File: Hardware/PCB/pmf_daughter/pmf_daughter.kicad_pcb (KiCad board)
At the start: 2 copper layers, 92.5 x 52 mm, 40 parts, among them J1 Conn_02x07_Odd_Even

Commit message: Font change; GND instead of NC on d-board
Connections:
- J1 pad 13: unconnected-(J1-Pin_13-Pad13) -> GND
- J1 pad 14: unconnected-(J1-Pin_14-Pad14) -> GND
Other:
- board text added: "POLE MIXING FILTER Expansion Board"
- board text added: "Rich Holmes / CC0 1.0"
- board text removed: "NC"
- board text removed: "Pole Mixing Filter Expansion Board Rich Holmes / CC0 1.0"

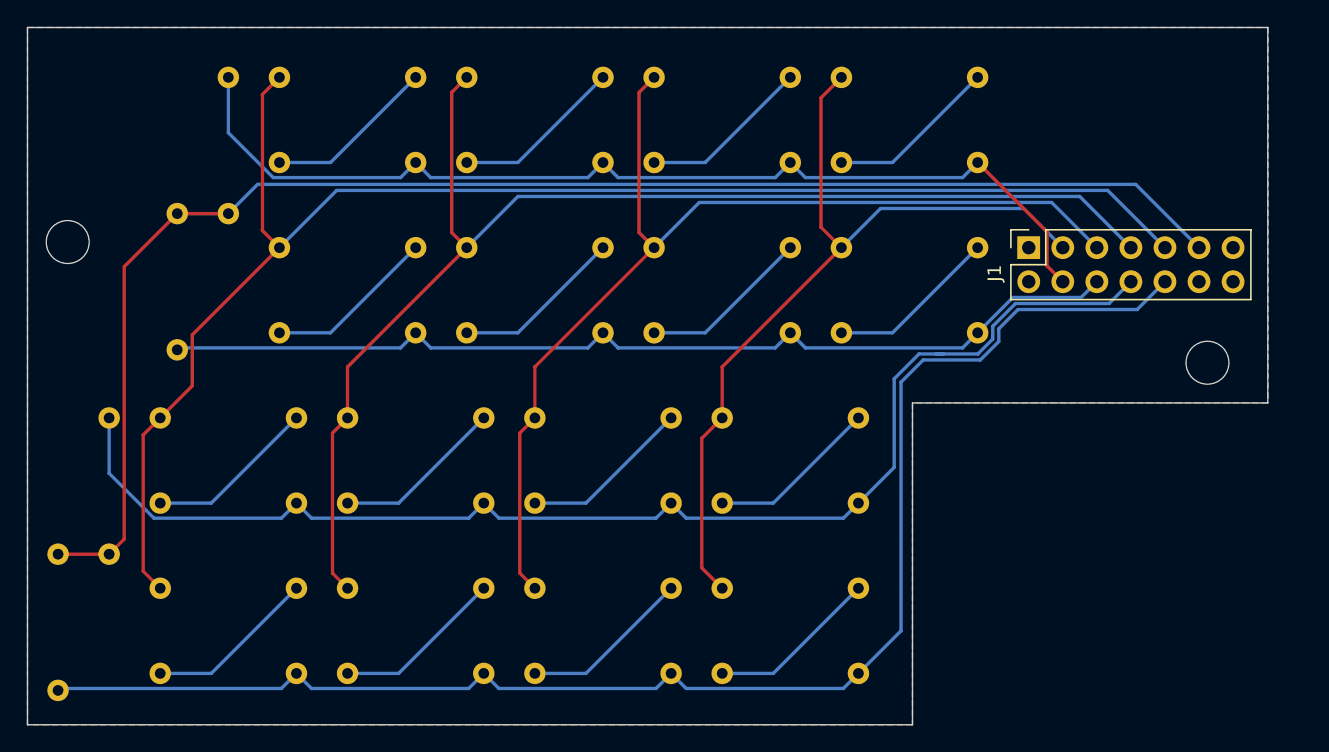
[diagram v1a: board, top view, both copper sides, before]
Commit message: Bigger trimmers for RC; slightly move expansion header
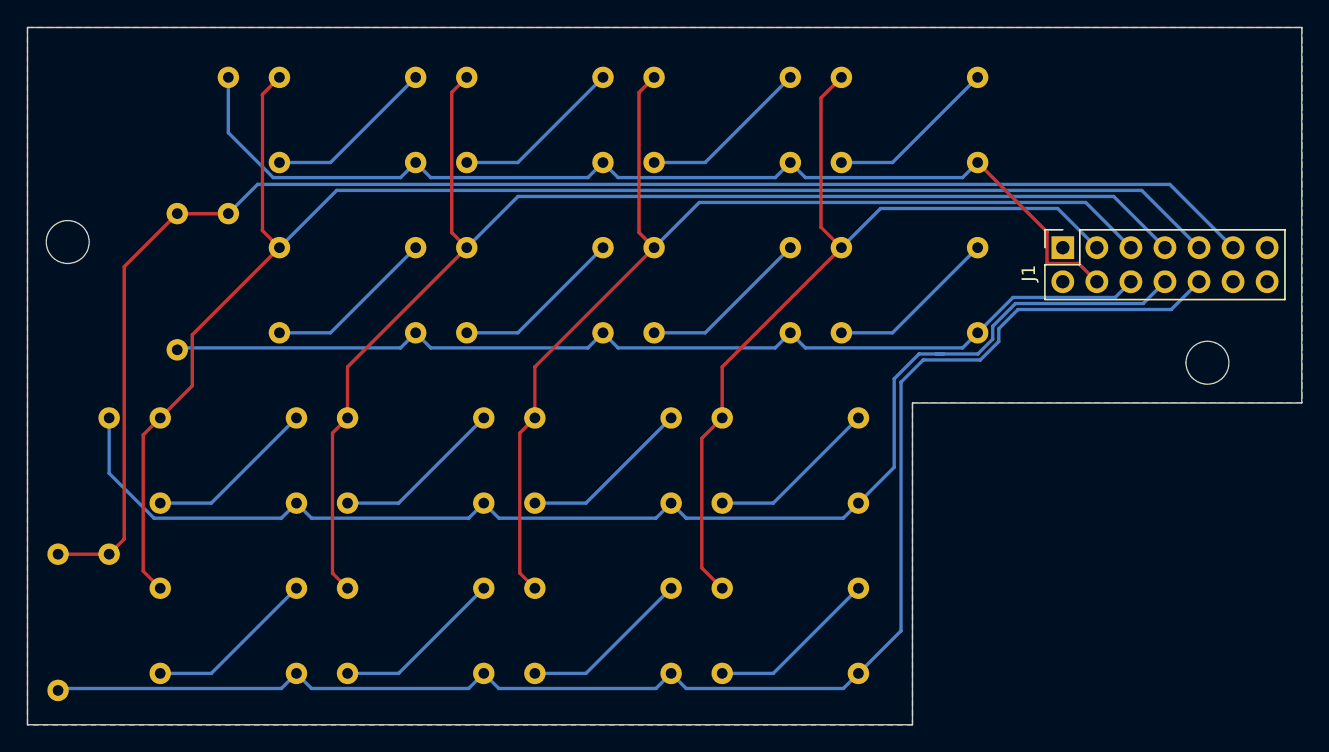
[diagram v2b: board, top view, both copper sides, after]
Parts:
- moved J1 2.54 mm to (129.2, 31.4)
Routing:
- net LINK2: track 96.8 -> 99.4 mm
- net LP2: track 96.3 -> 98.9 mm
- net LINK3: track 73.5 -> 76.0 mm
- net LINK1: track 109.4 -> 111.9 mm
- net LP4: track 63.2 -> 65.8 mm
- net LP3: track 79.5 -> 82.0 mm
- net INPUT: track 110.4 -> 112.9 mm
- net LP1: track 113.5 -> 116.0 mm
- net LINK4: track 76.2 -> 78.6 mm
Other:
- board size 92.5 x 52 mm -> 95 x 52 mm
